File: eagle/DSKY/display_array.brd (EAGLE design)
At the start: 160 x 100 mm, 65 parts, among them IC1 PCF8574T, IC10 PCF8574AT, IC2 PCF8574T, IC3 PCF8574T, IC4 PCF8574T, IC5 PCF8574T, IC6 PCF8574T, IC7 PCF8574T, IC8 PCF8574T, IC9 PCF8574AT

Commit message: brightness control
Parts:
- removed C1, C10, C2, C3, C4, C5, C6, C7, C8, C9: 100n, be_rcl:S_0805
- removed DIS1, DIS2, DIS3, DIS4, DIS5, DIS6, DIS7, DIS8: VQB71, be_opt:T_VQB71
- removed IC1, IC2, IC3, IC4, IC5, IC6, IC7, IC8: PCF8574T, be_i2c:S_SOIC16
- removed IC10, IC9: PCF8574AT, be_i2c:S_SOIC16
- removed LED1, LED12, LED4, LED5, LED7: red, be_opt:S_0805
- removed LED10, LED9: green, be_opt:S_0805
- removed LED2, LED3: blue, be_opt:S_0805
- removed LED6, LED8: yellow, be_opt:S_0805
- removed R1, R2, R3, R4, R5, R6, R7, R8, R9: (no value), be_rcl:S_0805
- removed RN1, RN10, RN11, RN12, RN13, RN14, RN15, RN16, RN2, RN3, RN4, RN5, RN6, RN7, RN8, RN9: 100, be_rcl:T_SIL8
- removed RN17: (no value), be_rcl:T_SIL9
- added C1001, C101, C1205, C1206, C1305, C1306, C201, C301, C401, C501, C601, C701, C801, C901: 100n, be_rcl:S_0805
- added C1201, C1202, C1203, C1204, C1301, C1302, C1303, C1304: 10u, be_rcl:T_RADIAL_5MM_GRID_2.54MM
- added DIS101, DIS201, DIS301, DIS401, DIS501, DIS601, DIS701, DIS801: VQB71, be_opt:T_VQB71
- added H1101, H1102, H1103, H1104: HOLE_4.1_PAD, be_holes:4.1_PAD
- added IC1001, IC901: PCF8574AT, be_i2c:S_SOIC16
- added IC101, IC201, IC301, IC401, IC501, IC601, IC701, IC801: PCF8574T, be_i2c:S_SOIC16
- added IC1201, IC1202, IC1301, IC1302: (no value), be_logic:T_NDIP14
- added LED901, LED902, LED907, LED910, LED911: red, be_opt:S_0805
- added LED903, LED904: green, be_opt:S_0805
- added LED905, LED906: yellow, be_opt:S_0805
- added LED908, LED909: blue, be_opt:S_0805
- added R901, R902, R903, R904, R905, R906, R907, R908, R909: (no value), be_rcl:S_0805
- added RN1001, RN1002, RN101, RN102, RN201, RN202, RN301, RN302, RN401, RN402, RN501, RN502, RN601, RN602, RN701, RN702, RN801, RN802: 100, be_rcl:T_SIL8
- added RN1201, RN1202, RN1301, RN1302: 220, be_rcl:T_SIL8
- added RN1203, RN1303: 4k7, be_rcl:T_SIL8
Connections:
- new net DEBOUNCER_10: C1201.+, RN1201.2, RN1201.3
- new net DEBOUNCER_11: IC1201.1, IC1201.2, RN1201.4, RN1203.3
- new net DEBOUNCER_12: IC1201.3, IC1201.4, IC1201.5
- new net DEBOUNCER_1_OUT#: IC1201.6, RN1001.2, RN1203.4
- new net DEBOUNCER_20: C1202.+, RN1201.6, RN1201.7
- new net DEBOUNCER_21: IC1201.12, IC1201.13, RN1201.8, RN1203.1
- new net DEBOUNCER_22: IC1201.10, IC1201.11, IC1201.9
- new net DEBOUNCER_2_OUT#: IC1201.8, RN1001.4, RN1203.2
- new net DEBOUNCER_30: C1203.+, RN1202.2, RN1202.3
- new net DEBOUNCER_31: IC1202.1, IC1202.2, RN1202.4, RN1203.5
- new net DEBOUNCER_32: IC1202.3, IC1202.4, IC1202.5
- new net DEBOUNCER_3_OUT#: IC1202.6, RN1001.6, RN1203.6
- new net DEBOUNCER_40: C1204.+, RN1202.6, RN1202.7
- new net DEBOUNCER_41: IC1202.12, IC1202.13, RN1202.8, RN1203.7
- new net DEBOUNCER_42: IC1202.10, IC1202.11, IC1202.9
- new net DEBOUNCER_4_OUT#: IC1202.8, RN1001.8, RN1203.8
- new net DEBOUNCER_50: C1301.+, RN1301.2, RN1301.3
- new net DEBOUNCER_51: IC1301.1, IC1301.2, RN1301.4, RN1303.3
- new net DEBOUNCER_52: IC1301.3, IC1301.4, IC1301.5
- new net DEBOUNCER_5_OUT#: IC1301.6, RN1002.2, RN1303.4
- new net DEBOUNCER_60: C1302.+, RN1301.6, RN1301.7
- new net DEBOUNCER_61: IC1301.12, IC1301.13, RN1301.8, RN1303.1
- new net DEBOUNCER_62: IC1301.10, IC1301.11, IC1301.9
- new net DEBOUNCER_6_OUT#: IC1301.8, RN1002.4, RN1303.2
- new net DEBOUNCER_70: C1303.+, RN1302.2, RN1302.3
- new net DEBOUNCER_71: IC1302.1, IC1302.2, RN1302.4, RN1303.5
- new net DEBOUNCER_72: IC1302.3, IC1302.4, IC1302.5
- new net DEBOUNCER_7_OUT#: IC1302.6, RN1002.6, RN1303.6
- new net DEBOUNCER_80: C1304.+, RN1302.6, RN1302.7
- new net DEBOUNCER_81: IC1302.12, IC1302.13, RN1302.8, RN1303.7
- new net DEBOUNCER_82: IC1302.10, IC1302.11, IC1302.9
- new net DEBOUNCER_8_OUT#: IC1302.8, RN1002.8, RN1303.8
- new net IN_1#: RN1201.1
- new net IN_2#: RN1201.5
- new net IN_3#: RN1202.1
- new net IN_4#: RN1202.5
- new net IN_5#: RN1301.1
- new net IN_6#: RN1301.5
- new net IN_7#: RN1302.1
- new net IN_8#: RN1302.5
- net CTRL_SCL: now also IC1001.14, IC101.14, IC201.14, IC301.14, IC401.14, IC501.14, IC601.14, IC701.14, IC801.14, IC901.14; no longer IC1.14, IC10.14, IC2.14, IC3.14, IC4.14, IC5.14, IC6.14, IC7.14, IC8.14, IC9.14
- net CTRL_SDA: now also IC1001.15, IC101.15, IC201.15, IC301.15, IC401.15, IC501.15, IC601.15, IC701.15, IC801.15, IC901.15; no longer IC1.15, IC10.15, IC2.15, IC3.15, IC4.15, IC5.15, IC6.15, IC7.15, IC8.15, IC9.15
- net DRV_1_SEG_A: now also IC101.4, RN101.1; no longer IC1.4, RN1.1
- net DRV_1_SEG_B: now also IC101.5, RN101.3; no longer IC1.5, RN1.3
- net DRV_1_SEG_C: now also IC101.6, RN101.5; no longer IC1.6, RN1.5
- net DRV_1_SEG_D: now also IC101.7, RN101.7; no longer IC1.7, RN1.7
- net DRV_1_SEG_E: now also IC101.9, RN102.1; no longer IC1.9, RN2.1
- net DRV_1_SEG_F: now also IC101.10, RN102.3; no longer IC1.10, RN2.3
- net DRV_1_SEG_G: now also IC101.11, RN102.5; no longer IC1.11, RN2.5
- net DRV_1_SEG_H: now also IC101.12, RN102.7; no longer IC1.12, RN2.7
- net DRV_1_SEG_RA: now also DIS101.7, RN101.2; no longer DIS1.7, RN1.2
- net DRV_1_SEG_RB: now also DIS101.6, RN101.4; no longer DIS1.6, RN1.4
- net DRV_1_SEG_RC: now also DIS101.4, RN101.6; no longer DIS1.4, RN1.6
- net DRV_1_SEG_RD: now also DIS101.2, RN101.8; no longer DIS1.2, RN1.8
- net DRV_1_SEG_RE: now also DIS101.1, RN102.2; no longer DIS1.1, RN2.2
- net DRV_1_SEG_RF: now also DIS101.10, RN102.4; no longer DIS1.10, RN2.4
- net DRV_1_SEG_RG: now also DIS101.9, RN102.6; no longer DIS1.9, RN2.6
- net DRV_1_SEG_RH: now also DIS101.5, RN102.8; no longer DIS1.5, RN2.8
- net DRV_2_SEG_A: now also IC201.4, RN201.1; no longer IC2.4, RN3.1
- net DRV_2_SEG_B: now also IC201.5, RN201.3; no longer IC2.5, RN3.3
- net DRV_2_SEG_C: now also IC201.6, RN201.5; no longer IC2.6, RN3.5
- net DRV_2_SEG_D: now also IC201.7, RN201.7; no longer IC2.7, RN3.7
- net DRV_2_SEG_E: now also IC201.9, RN202.1; no longer IC2.9, RN4.1
- net DRV_2_SEG_F: now also IC201.10, RN202.3; no longer IC2.10, RN4.3
- net DRV_2_SEG_G: now also IC201.11, RN202.5; no longer IC2.11, RN4.5
- net DRV_2_SEG_H: now also IC201.12, RN202.7; no longer IC2.12, RN4.7
- net DRV_2_SEG_RA: now also DIS201.7, RN201.2; no longer DIS2.7, RN3.2
- net DRV_2_SEG_RB: now also DIS201.6, RN201.4; no longer DIS2.6, RN3.4
- net DRV_2_SEG_RC: now also DIS201.4, RN201.6; no longer DIS2.4, RN3.6
- net DRV_2_SEG_RD: now also DIS201.2, RN201.8; no longer DIS2.2, RN3.8
- net DRV_2_SEG_RE: now also DIS201.1, RN202.2; no longer DIS2.1, RN4.2
- net DRV_2_SEG_RF: now also DIS201.10, RN202.4; no longer DIS2.10, RN4.4
- net DRV_2_SEG_RG: now also DIS201.9, RN202.6; no longer DIS2.9, RN4.6
- net DRV_2_SEG_RH: now also DIS201.5, RN202.8; no longer DIS2.5, RN4.8
- net DRV_3_SEG_A: now also IC301.4, RN301.1; no longer IC3.4, RN5.1
- net DRV_3_SEG_B: now also IC301.5, RN301.3; no longer IC3.5, RN5.3
- net DRV_3_SEG_C: now also IC301.6, RN301.5; no longer IC3.6, RN5.5
- net DRV_3_SEG_D: now also IC301.7, RN301.7; no longer IC3.7, RN5.7
- net DRV_3_SEG_E: now also IC301.9, RN302.1; no longer IC3.9, RN6.1
- net DRV_3_SEG_F: now also IC301.10, RN302.3; no longer IC3.10, RN6.3
- net DRV_3_SEG_G: now also IC301.11, RN302.5; no longer IC3.11, RN6.5
- net DRV_3_SEG_H: now also IC301.12, RN302.7; no longer IC3.12, RN6.7
- net DRV_3_SEG_RA: now also DIS301.7, RN301.2; no longer DIS3.7, RN5.2
- net DRV_3_SEG_RB: now also DIS301.6, RN301.4; no longer DIS3.6, RN5.4
- net DRV_3_SEG_RC: now also DIS301.4, RN301.6; no longer DIS3.4, RN5.6
- net DRV_3_SEG_RD: now also DIS301.2, RN301.8; no longer DIS3.2, RN5.8
- net DRV_3_SEG_RE: now also DIS301.1, RN302.2; no longer DIS3.1, RN6.2
- net DRV_3_SEG_RF: now also DIS301.10, RN302.4; no longer DIS3.10, RN6.4
- net DRV_3_SEG_RG: now also DIS301.9, RN302.6; no longer DIS3.9, RN6.6
- net DRV_3_SEG_RH: now also DIS301.5, RN302.8; no longer DIS3.5, RN6.8
- net DRV_4_SEG_A: now also IC401.4, RN401.1; no longer IC4.4, RN7.1
- net DRV_4_SEG_B: now also IC401.5, RN401.3; no longer IC4.5, RN7.3
- net DRV_4_SEG_C: now also IC401.6, RN401.5; no longer IC4.6, RN7.5
- net DRV_4_SEG_D: now also IC401.7, RN401.7; no longer IC4.7, RN7.7
- net DRV_4_SEG_E: now also IC401.9, RN402.1; no longer IC4.9, RN8.1
- net DRV_4_SEG_F: now also IC401.10, RN402.3; no longer IC4.10, RN8.3
- net DRV_4_SEG_G: now also IC401.11, RN402.5; no longer IC4.11, RN8.5
- net DRV_4_SEG_H: now also IC401.12, RN402.7; no longer IC4.12, RN8.7
- net DRV_4_SEG_RA: now also DIS401.7, RN401.2; no longer DIS4.7, RN7.2
- net DRV_4_SEG_RB: now also DIS401.6, RN401.4; no longer DIS4.6, RN7.4
- net DRV_4_SEG_RC: now also DIS401.4, RN401.6; no longer DIS4.4, RN7.6
- net DRV_4_SEG_RD: now also DIS401.2, RN401.8; no longer DIS4.2, RN7.8
- net DRV_4_SEG_RE: now also DIS401.1, RN402.2; no longer DIS4.1, RN8.2
- net DRV_4_SEG_RF: now also DIS401.10, RN402.4; no longer DIS4.10, RN8.4
- net DRV_4_SEG_RG: now also DIS401.9, RN402.6; no longer DIS4.9, RN8.6
- net DRV_4_SEG_RH: now also DIS401.5, RN402.8; no longer DIS4.5, RN8.8
- net DRV_5_SEG_A: now also IC501.4, RN501.1; no longer IC5.4, RN9.1
- net DRV_5_SEG_B: now also IC501.5, RN501.3; no longer IC5.5, RN9.3
- net DRV_5_SEG_C: now also IC501.6, RN501.5; no longer IC5.6, RN9.5
- net DRV_5_SEG_D: now also IC501.7, RN501.7; no longer IC5.7, RN9.7
- net DRV_5_SEG_E: now also IC501.9, RN502.1; no longer IC5.9, RN10.1
- net DRV_5_SEG_F: now also IC501.10, RN502.3; no longer IC5.10, RN10.3
- net DRV_5_SEG_G: now also IC501.11, RN502.5; no longer IC5.11, RN10.5
- net DRV_5_SEG_H: now also IC501.12, RN502.7; no longer IC5.12, RN10.7
- net DRV_5_SEG_RA: now also DIS501.7, RN501.2; no longer DIS5.7, RN9.2
- net DRV_5_SEG_RB: now also DIS501.6, RN501.4; no longer DIS5.6, RN9.4
- net DRV_5_SEG_RC: now also DIS501.4, RN501.6; no longer DIS5.4, RN9.6
- net DRV_5_SEG_RD: now also DIS501.2, RN501.8; no longer DIS5.2, RN9.8
- net DRV_5_SEG_RE: now also DIS501.1, RN502.2; no longer DIS5.1, RN10.2
- net DRV_5_SEG_RF: now also DIS501.10, RN502.4; no longer DIS5.10, RN10.4
- net DRV_5_SEG_RG: now also DIS501.9, RN502.6; no longer DIS5.9, RN10.6
- net DRV_5_SEG_RH: now also DIS501.5, RN502.8; no longer DIS5.5, RN10.8
- net DRV_6_SEG_A: now also IC601.4, RN601.1; no longer IC6.4, RN11.1
- net DRV_6_SEG_B: now also IC601.5, RN601.3; no longer IC6.5, RN11.3
- net DRV_6_SEG_C: now also IC601.6, RN601.5; no longer IC6.6, RN11.5
- net DRV_6_SEG_D: now also IC601.7, RN601.7; no longer IC6.7, RN11.7
- net DRV_6_SEG_E: now also IC601.9, RN602.1; no longer IC6.9, RN12.1
- net DRV_6_SEG_F: now also IC601.10, RN602.3; no longer IC6.10, RN12.3
- net DRV_6_SEG_G: now also IC601.11, RN602.5; no longer IC6.11, RN12.5
- net DRV_6_SEG_H: now also IC601.12, RN602.7; no longer IC6.12, RN12.7
- net DRV_6_SEG_RA: now also DIS601.7, RN601.2; no longer DIS6.7, RN11.2
- net DRV_6_SEG_RB: now also DIS601.6, RN601.4; no longer DIS6.6, RN11.4
- net DRV_6_SEG_RC: now also DIS601.4, RN601.6; no longer DIS6.4, RN11.6
- net DRV_6_SEG_RD: now also DIS601.2, RN601.8; no longer DIS6.2, RN11.8
- net DRV_6_SEG_RE: now also DIS601.1, RN602.2; no longer DIS6.1, RN12.2
- net DRV_6_SEG_RF: now also DIS601.10, RN602.4; no longer DIS6.10, RN12.4
- net DRV_6_SEG_RG: now also DIS601.9, RN602.6; no longer DIS6.9, RN12.6
- net DRV_6_SEG_RH: now also DIS601.5, RN602.8; no longer DIS6.5, RN12.8
- net DRV_7_SEG_A: now also IC701.4, RN701.1; no longer IC7.4, RN13.1
- net DRV_7_SEG_B: now also IC701.5, RN701.3; no longer IC7.5, RN13.3
- net DRV_7_SEG_C: now also IC701.6, RN701.5; no longer IC7.6, RN13.5
- net DRV_7_SEG_D: now also IC701.7, RN701.7; no longer IC7.7, RN13.7
- net DRV_7_SEG_E: now also IC701.9, RN702.1; no longer IC7.9, RN14.1
- net DRV_7_SEG_F: now also IC701.10, RN702.3; no longer IC7.10, RN14.3
- net DRV_7_SEG_G: now also IC701.11, RN702.5; no longer IC7.11, RN14.5
- net DRV_7_SEG_H: now also IC701.12, RN702.7; no longer IC7.12, RN14.7
- net DRV_7_SEG_RA: now also DIS701.7, RN701.2; no longer DIS7.7, RN13.2
- net DRV_7_SEG_RB: now also DIS701.6, RN701.4; no longer DIS7.6, RN13.4
- net DRV_7_SEG_RC: now also DIS701.4, RN701.6; no longer DIS7.4, RN13.6
- net DRV_7_SEG_RD: now also DIS701.2, RN701.8; no longer DIS7.2, RN13.8
- net DRV_7_SEG_RE: now also DIS701.1, RN702.2; no longer DIS7.1, RN14.2
- net DRV_7_SEG_RF: now also DIS701.10, RN702.4; no longer DIS7.10, RN14.4
- net DRV_7_SEG_RG: now also DIS701.9, RN702.6; no longer DIS7.9, RN14.6
- net DRV_7_SEG_RH: now also DIS701.5, RN702.8; no longer DIS7.5, RN14.8
- net DRV_8_SEG_A: now also IC801.4, RN801.1; no longer IC8.4, RN15.1
- net DRV_8_SEG_B: now also IC801.5, RN801.3; no longer IC8.5, RN15.3
- net DRV_8_SEG_C: now also IC801.6, RN801.5; no longer IC8.6, RN15.5
- net DRV_8_SEG_D: now also IC801.7, RN801.7; no longer IC8.7, RN15.7
- net DRV_8_SEG_E: now also IC801.9, RN802.1; no longer IC8.9, RN16.1
- net DRV_8_SEG_F: now also IC801.10, RN802.3; no longer IC8.10, RN16.3
- net DRV_8_SEG_G: now also IC801.11, RN802.5; no longer IC8.11, RN16.5
- net DRV_8_SEG_H: now also IC801.12, RN802.7; no longer IC8.12, RN16.7
- net DRV_8_SEG_RA: now also DIS801.7, RN801.2; no longer DIS8.7, RN15.2
- net DRV_8_SEG_RB: now also DIS801.6, RN801.4; no longer DIS8.6, RN15.4
- net DRV_8_SEG_RC: now also DIS801.4, RN801.6; no longer DIS8.4, RN15.6
- net DRV_8_SEG_RD: now also DIS801.2, RN801.8; no longer DIS8.2, RN15.8
- net DRV_8_SEG_RE: now also DIS801.1, RN802.2; no longer DIS8.1, RN16.2
- net DRV_8_SEG_RF: now also DIS801.10, RN802.4; no longer DIS8.10, RN16.4
- net DRV_8_SEG_RG: now also DIS801.9, RN802.6; no longer DIS8.9, RN16.6
- net DRV_8_SEG_RH: now also DIS801.5, RN802.8; no longer DIS8.5, RN16.8
- net DRV_9_LED_1: now also IC901.4, R901.1, R902.1; no longer IC9.4, R8.1, R9.1
- net DRV_9_LED_2: now also IC901.5, R903.1; no longer IC9.5, R7.1
- net DRV_9_LED_3: now also IC901.6, R904.1; no longer IC9.6, R6.1
- net DRV_9_LED_4: now also IC901.7, R905.1; no longer IC9.7, R5.1
- net DRV_9_LED_5: now also IC901.9, R906.1; no longer IC9.9, R4.1
- net DRV_9_LED_6: now also IC901.10, R907.1; no longer IC9.10, R3.1
- net DRV_9_LED_7: now also IC901.11, R908.1; no longer IC9.11, R2.1
- net DRV_9_LED_8: now also IC901.12, R909.1; no longer IC9.12, R1.1
- net DRV_9_LED_R1A: now also LED901.C, R901.2; no longer LED5.C, R9.2
- net DRV_9_LED_R1B: now also LED902.C, R902.2; no longer LED1.C, R8.2
- net DRV_9_LED_R2: now also LED903.C, R903.2; no longer LED10.C, R7.2
- net DRV_9_LED_R3: now also LED904.C, R904.2; no longer LED9.C, R6.2
- net DRV_9_LED_R4: now also LED905.C, R905.2; no longer LED8.C, R5.2
- net DRV_9_LED_R5: now also LED906.C, R906.2; no longer LED6.C, R4.2
- net DRV_9_LED_R6: now also LED907.C, R907.2; no longer LED7.C, R3.2
- net DRV_9_LED_R7: now also LED908.C, R908.2; no longer LED3.C, R2.2
- net DRV_9_LED_R8: now also LED909.C, R909.2; no longer LED2.C, R1.2
- net DRV_ANODE: now also DIS101.3, DIS101.8, DIS201.3, DIS201.8, DIS301.3, DIS301.8, DIS401.3, DIS401.8, DIS501.3, DIS501.8, DIS601.3, DIS601.8, DIS701.3, DIS701.8, DIS801.3, DIS801.8, LED903.A, LED904.A, LED905.A, LED906.A, LED907.A, LED908.A, LED909.A, LED910.A, LED911.A; no longer DIS1.3, DIS1.8, DIS2.3, DIS2.8, DIS3.3, DIS3.8, DIS4.3, DIS4.8, DIS5.3, DIS5.8, DIS6.3, DIS6.8, DIS7.3, DIS7.8, DIS8.3, DIS8.8
- net GND: now also C1001.1, C101.1, C1201.-, C1202.-, C1203.-, C1204.-, C1205.2, C1206.2, C1301.-, C1302.-, C1303.-, C1304.-, C1305.2, C1306.2, C201.1, C301.1, C401.1, C501.1, C601.1, C701.1, C801.1, C901.1, IC1001.2, IC1001.3, IC1001.8, IC101.1, IC101.2, IC101.3, IC101.8, IC1201.7, IC1202.7, IC1301.7, IC1302.7, IC201.2, IC201.3, IC201.8, IC301.1, IC301.3, IC301.8, IC401.3, IC401.8, IC501.1, IC501.2, IC501.8, IC601.2, IC601.8, IC701.1, IC701.8, IC801.8, IC901.1, IC901.2, IC901.3, IC901.8; no longer C1.1, C10.1, C2.1, C3.1, C4.1, C5.1, C6.1, C7.1, C8.1, C9.1, IC1.1, IC1.2, IC1.3, IC1.8, IC10.2, IC10.3, IC10.8, IC2.2, IC2.3, IC2.8, IC3.1, IC3.3, IC3.8, IC4.3, IC4.8, IC5.1, IC5.2, IC5.8, IC6.2, IC6.8, IC7.1, IC7.8, IC8.8, IC9.1, IC9.2, IC9.3, IC9.8
- net KEYPAD_1_K_1: now also IC1001.4, RN1001.1; no longer IC10.4, RN17.2
- net KEYPAD_1_K_2: now also IC1001.5, RN1001.3; no longer IC10.5, RN17.3
- net KEYPAD_1_K_3: now also IC1001.6, RN1001.5; no longer IC10.6, RN17.4
- net KEYPAD_1_K_4: now also IC1001.7, RN1001.7; no longer IC10.7, RN17.5
- net KEYPAD_1_K_5: now also IC1001.9, RN1002.1; no longer IC10.9, RN17.6
- net KEYPAD_1_K_6: now also IC1001.10, RN1002.3; no longer IC10.10, RN17.7
- net KEYPAD_1_K_7: now also IC1001.11, RN1002.5; no longer IC10.11, RN17.8
- net KEYPAD_1_K_8: now also IC1001.12, RN1002.7; no longer IC10.12, RN17.9
- net N$1: now also LED902.A, LED911.C; no longer LED1.A, LED4.C
- net N$2: now also LED901.A, LED910.C; no longer LED12.C, LED5.A
- net P5V: now also C1001.2, C101.2, C1205.1, C1206.1, C1305.1, C1306.1, C201.2, C301.2, C401.2, C501.2, C601.2, C701.2, C801.2, C901.2, IC1001.1, IC1001.16, IC101.16, IC1201.14, IC1202.14, IC1301.14, IC1302.14, IC201.1, IC201.16, IC301.16, IC301.2, IC401.1, IC401.16, IC401.2, IC501.16, IC501.3, IC601.1, IC601.16, IC601.3, IC701.16, IC701.2, IC701.3, IC801.1, IC801.16, IC801.2, IC801.3, IC901.16; no longer C1.2, C10.2, C2.2, C3.2, C4.2, C5.2, C6.2, C7.2, C8.2, C9.2, IC1.16, IC10.1, IC10.16, IC2.1, IC2.16, IC3.16, IC3.2, IC4.1, IC4.16, IC4.2, IC5.16, IC5.3, IC6.1, IC6.16, IC6.3, IC7.16, IC7.2, IC7.3, IC8.1, IC8.16, IC8.2, IC8.3, IC9.16, LED10.A, LED12.A, LED2.A, LED3.A, LED4.A, LED6.A, LED7.A, LED8.A, LED9.A, RN17.1
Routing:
- net DRV_ANODE: track 140.0 -> 294.7 mm, vias 0 -> 3
- net DRV_9_LED_1: track 20.3 -> 164.2 mm
- net DEBOUNCER_6_OUT#: track 0.00 -> 121.5 mm, vias 0 -> 1
- net DEBOUNCER_7_OUT#: track 0.00 -> 117.0 mm, vias 0 -> 1
- net DEBOUNCER_5_OUT#: track 0.00 -> 109.0 mm
- net DEBOUNCER_8_OUT#: track 0.00 -> 104.5 mm
- net DEBOUNCER_2_OUT#: track 0.00 -> 93.2 mm, vias 0 -> 2
- net DEBOUNCER_1_OUT#: track 0.00 -> 84.1 mm, vias 0 -> 1
- net DEBOUNCER_3_OUT#: track 0.00 -> 73.7 mm, vias 0 -> 1
- net GND: track 125.1 -> 196.4 mm, vias 36 -> 44
- net DEBOUNCER_4_OUT#: track 0.00 -> 48.8 mm, vias 0 -> 1
- net DEBOUNCER_61: track 0.00 -> 46.0 mm
- net DEBOUNCER_21: track 0.00 -> 46.0 mm
- net DRV_9_LED_R2: track 0.00 -> 41.6 mm, vias 0 -> 2
- net DEBOUNCER_80: track 0.00 -> 40.8 mm
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- added copper zone on layer 1, net P5V

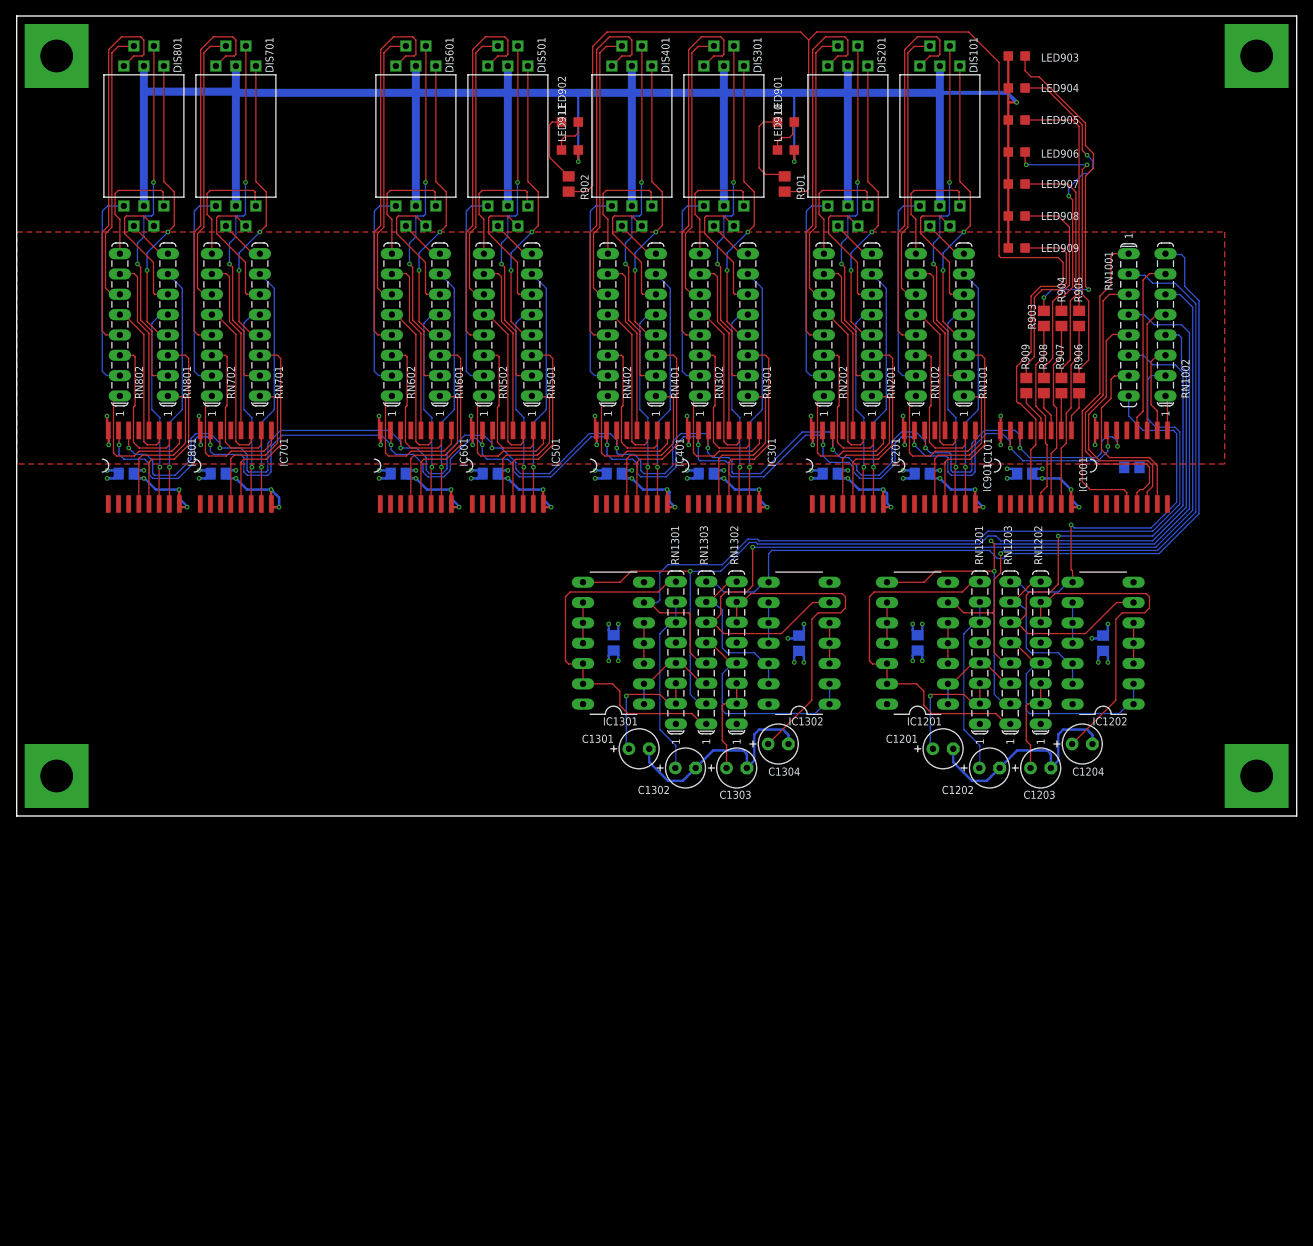
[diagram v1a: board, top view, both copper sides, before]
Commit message: added connectors
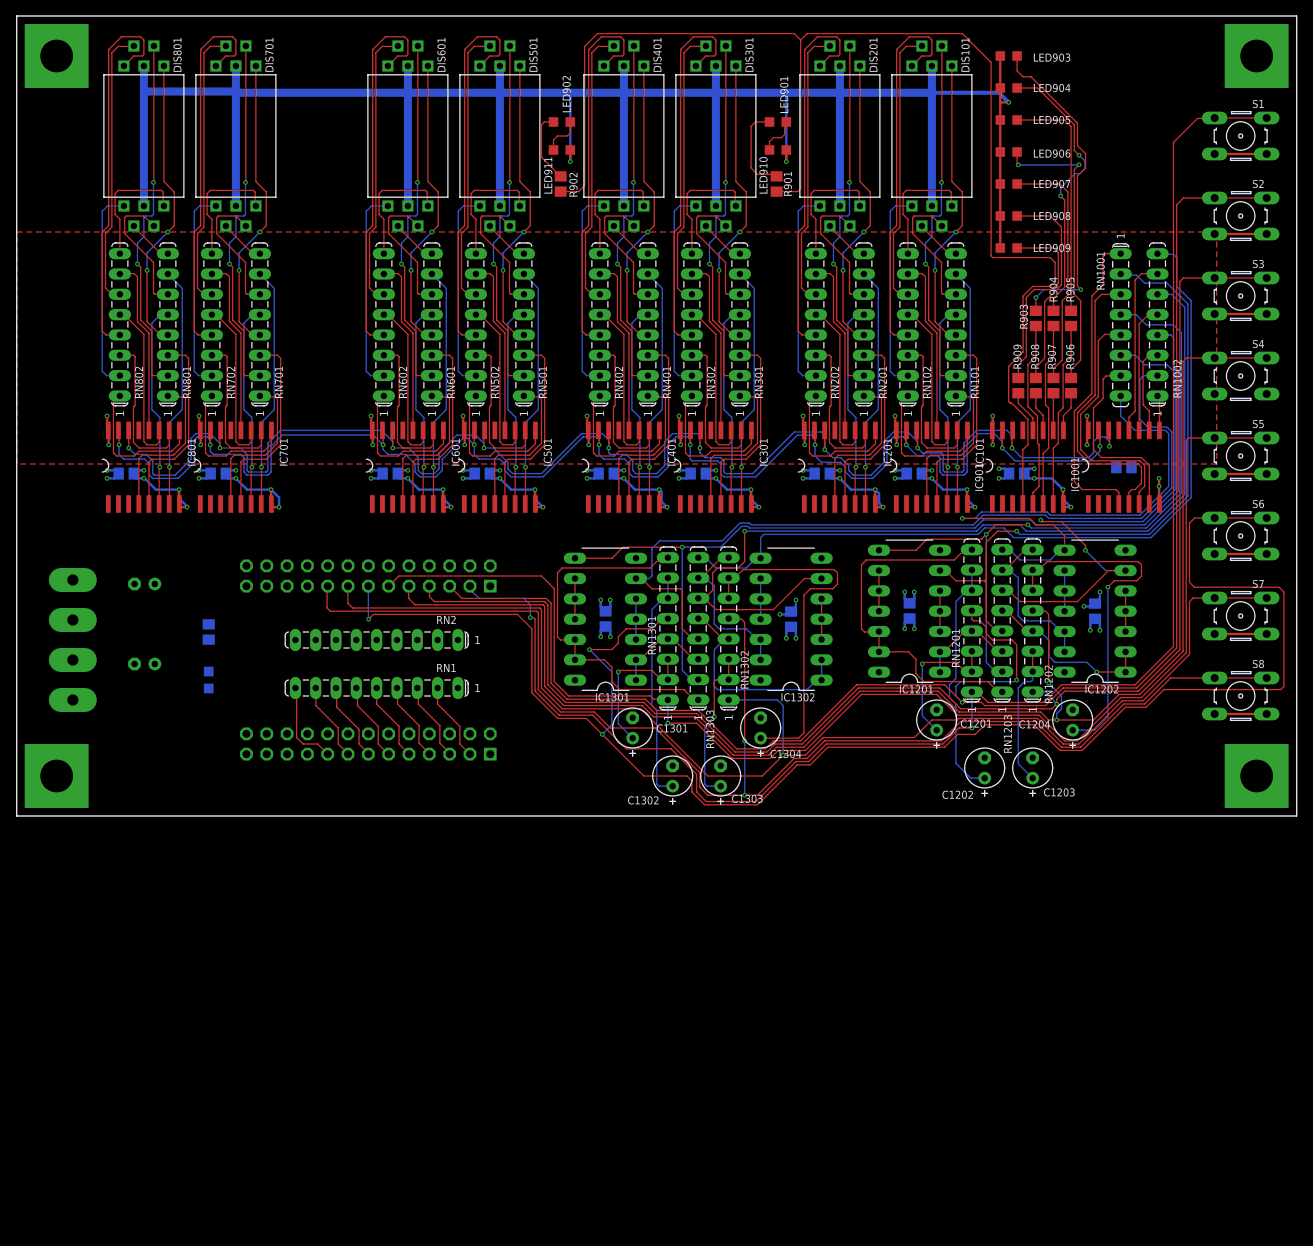
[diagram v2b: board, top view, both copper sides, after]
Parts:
- added C1, C2: 100u, be_rcl:T_RADIAL_7MM_GRID_2.54MM
- added LED1: green, be_opt:S_0805
- added R1: 220, be_rcl:S_0805
- added RN1, RN2: (no value), be_rcl:T_SIL9
- added S1, S2, S3, S4, S5, S6, S7, S8: (no value), be_switch:T_PUSH_BUTTON_6X6
- added X1, X3: MALE_2X13-T-VERTICAL_2.54MM, be_con_jump:T_MALE_2X13_VERTICAL_GRID_2.54MM
- added X2: CLAMP_1X4-T-5MM, be_con_jump:T_WIRE_CLAMP_1X4_5MM
- moved C1205 4.12 mm to (111.6, 25.6)
- moved C1206 4.12 mm to (134.8, 25.6)
- moved IC1201 4.12 mm to (111.6, 25.6)
- moved IC1202 4.12 mm to (134.8, 25.6)
- moved RN1201 4.12 mm to (119.4, 24.4)
- moved RN1202 4.12 mm to (127.0, 24.4)
- moved RN1203 4.12 mm to (123.2, 24.4)
- moved C1201 3.69 mm to (115.0, 12.0), turned to 90 degrees
- moved C1204 3.23 mm to (132.0, 12.0), turned to 90 degrees
- moved C1305 3.16 mm to (73.6, 24.6)
- moved C1306 3.16 mm to (96.8, 24.6)
- moved IC1301 3.16 mm to (73.6, 24.6)
- moved IC1302 3.16 mm to (96.8, 24.6)
- moved RN1301 3.16 mm to (81.4, 23.4)
- moved RN1302 3.16 mm to (89.0, 23.4)
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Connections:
- new net CTRL_ACK#: RN2.3, X1.19
- new net CTRL_B2: RN1.4, X1.7
- new net CTRL_B3: RN1.5, X1.9
- new net CTRL_B4: RN1.6, X1.11
- new net CTRL_B5: RN1.7, X1.13
- new net CTRL_B6: RN1.8, X1.15
- new net CTRL_B7: RN1.9, X1.17
- new net CTRL_BUSY: RN2.4, X1.21
- new net CTRL_STROBE#: RN2.2, X1.1
- new net P5V_LED: LED1.C, R1.2
- net CTRL_SCL: now also RN1.2, X1.3
- net CTRL_SDA: now also RN1.3, X1.5
- net GND: now also C1.-, C2.-, R1.1, S1.1, S1.3, S2.1, S2.3, S3.1, S3.3, S4.1, S4.3, S5.1, S5.3, S6.1, S6.3, S7.1, S7.3, S8.1, S8.3, X1.10, X1.12, X1.14, X1.16, X1.18, X1.2, X1.20, X1.22, X1.24, X1.26, X1.4, X1.6, X1.8, X2.3, X2.4, X3.10, X3.12, X3.14, X3.16, X3.18, X3.2, X3.20, X3.22, X3.24, X3.26, X3.4, X3.6, X3.8
- net IN_1#: now also S1.2, S1.4, X3.3
- net IN_2#: now also S2.2, S2.4, X3.5
- net IN_3#: now also S3.2, S3.4, X3.7
- net IN_4#: now also S4.2, S4.4, X3.9
- net IN_5#: now also S5.2, S5.4, X3.11
- net IN_6#: now also S6.2, S6.4, X3.13
- net IN_7#: now also S7.2, S7.4, X3.15
- net IN_8#: now also S8.2, S8.4, X3.17
- net P5V: now also C1.+, C2.+, LED1.A, RN1.1, RN2.1, X2.1, X2.2
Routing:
- net IN_6#: track 0.00 -> 208.5 mm, vias 0 -> 3
- net IN_2#: track 0.00 -> 202.7 mm, vias 0 -> 2
- net IN_1#: track 0.00 -> 194.5 mm, vias 0 -> 2
- net IN_4#: track 0.00 -> 183.8 mm, vias 0 -> 2
- net IN_3#: track 0.00 -> 177.6 mm, vias 0 -> 1
- net IN_8#: track 0.00 -> 169.1 mm, vias 0 -> 2
- net IN_5#: track 0.00 -> 165.2 mm, vias 0 -> 1
- net IN_7#: track 0.00 -> 160.7 mm, vias 0 -> 1
- net DEBOUNCER_4_OUT#: track 48.8 -> 68.1 mm
- net CTRL_B7: track 0.00 -> 11.0 mm
- net CTRL_B4: track 0.00 -> 9.96 mm
- net CTRL_B6: track 0.00 -> 9.94 mm
- net CTRL_B5: track 0.00 -> 9.94 mm
- net CTRL_B3: track 0.00 -> 9.94 mm
- net CTRL_B2: track 0.00 -> 9.94 mm
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
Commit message: reverse voltage protection
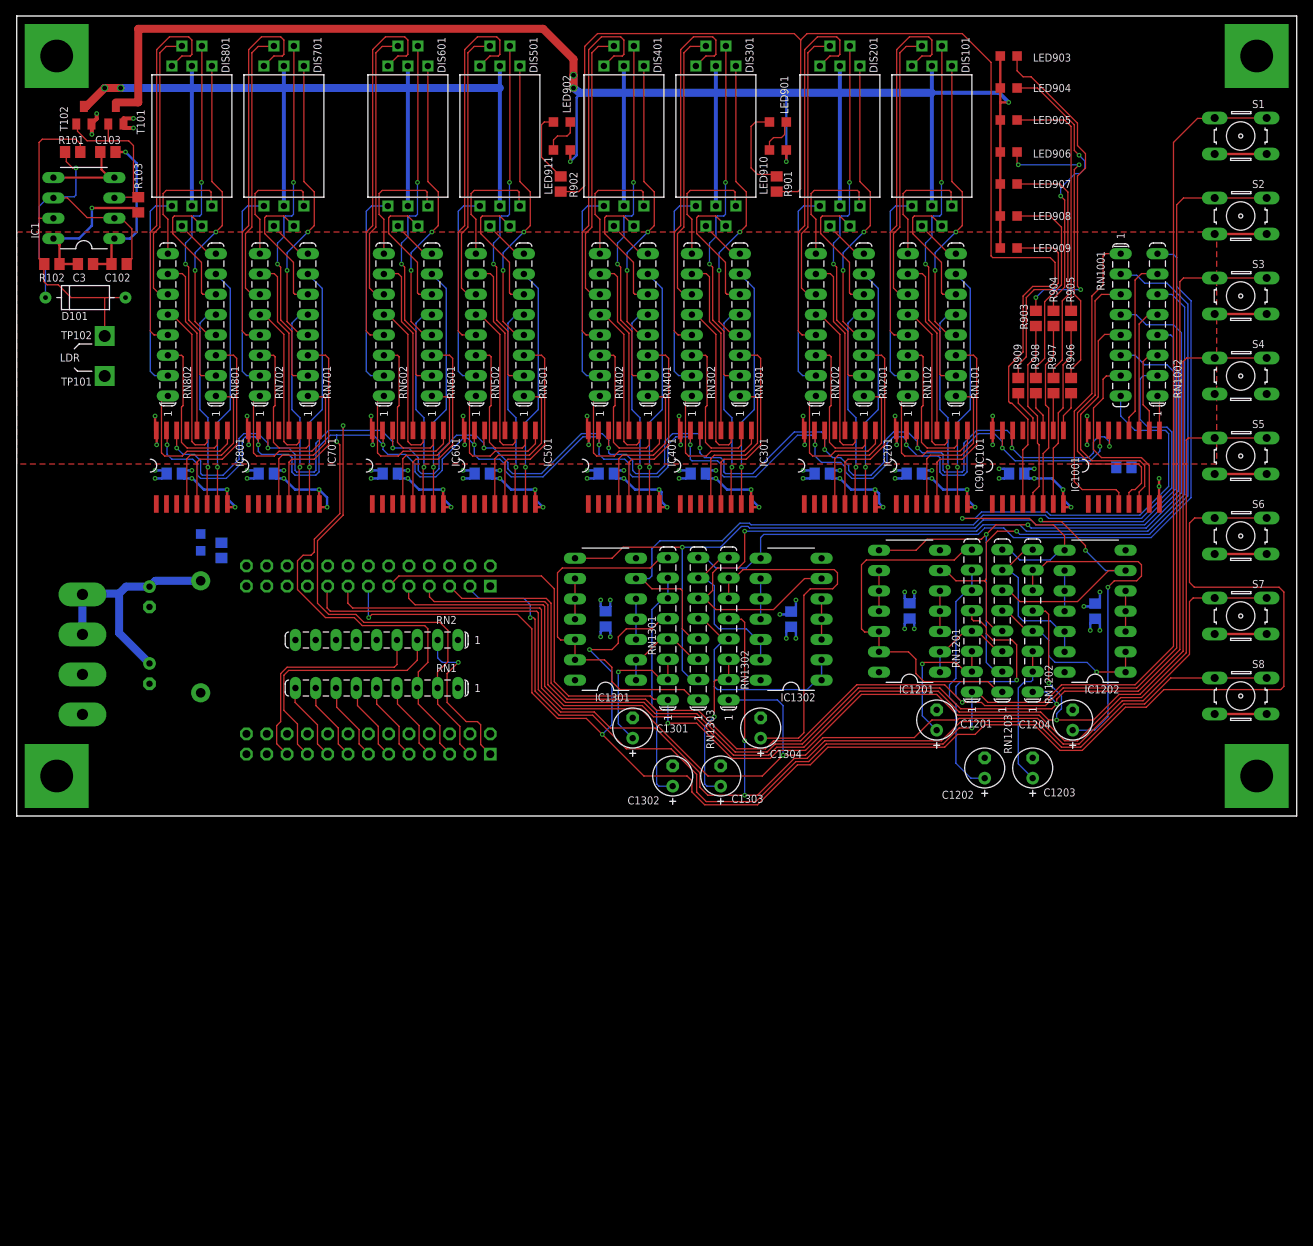
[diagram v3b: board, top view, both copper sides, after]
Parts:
- added C102: 47n, be_rcl:S_0805
- added C103: 10n, be_rcl:S_0805
- added C3: 100n, be_rcl:S_0805
- added D1: (no value), be_diode:T_DO204-2_GRID_14MM
- added D101: BAT48, be_diode:T_DO204_GRID_10MM
- added IC1: NE555V, be_timer:T_NDIP8
- added R101: 10k, be_rcl:S_0805
- added R102: 470k, be_rcl:S_0805
- added R103: 1k, be_rcl:S_0805
- added T101, T102: NX2301P, be_transistor:S_SOT23
- added TP101, TP102: (no value), be_con_jump:T_TEST_POINT_LARGE
- moved LED1 17.2 mm to (23.0, 34.2)
- moved R1 10.3 mm to (25.6, 33.2)
- moved C701 6.00 mm to (31.2, 42.8)
- moved C801 6.00 mm to (19.7, 42.8)
- moved DIS701 6.00 mm to (33.4, 85.0)
- moved IC701 6.00 mm to (33.4, 43.6)
- moved RN701 6.00 mm to (36.4, 61.4)
- moved RN702 6.00 mm to (30.4, 61.4)
- moved RN801 6.00 mm to (24.9, 61.4)
- moved DIS801 6.00 mm to (21.9, 85.0)
- moved IC801 6.00 mm to (21.9, 43.6)
- moved RN802 6.00 mm to (18.9, 61.4)
- moved X2 2.16 mm to (8.20, 20.2)
- moved C1 1.71 mm to (16.6, 27.4), turned to 270 degrees
- moved C2 1.34 mm to (16.6, 17.8), turned to 270 degrees
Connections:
- removed net DRV_ANODE: DIS101.3, DIS101.8, DIS201.3, DIS201.8, DIS301.3, DIS301.8, DIS401.3, DIS401.8, DIS501.3, DIS501.8, DIS601.3, DIS601.8, DIS701.3, DIS701.8, DIS801.3, DIS801.8, LED903.A, LED904.A, LED905.A, LED906.A, LED907.A, LED908.A, LED909.A, LED910.A, LED911.A
- new net DRV_ANODE_1: DIS101.3, DIS101.8, DIS201.3, DIS201.8, DIS301.3, DIS301.8, DIS401.3, DIS401.8, LED903.A, LED904.A, LED905.A, LED906.A, LED907.A, LED908.A, LED909.A, LED910.A, LED911.A, T101.3
- new net DRV_ANODE_2: DIS501.3, DIS501.8, DIS601.3, DIS601.8, DIS701.3, DIS701.8, DIS801.3, DIS801.8, T102.3
- new net TIM_1: C103.1, IC1.4, IC1.5
- new net TIM_2: C102.1, D101.C, IC1.2, IC1.6, R101.1
- new net TIM_3: D101.A, IC1.7, R101.2, R102.1, TP102.1
- new net TIM_OUT: IC1.3, R103.1, T101.1, T102.1
- net GND: now also C102.2, C103.2, C3.2, D1.A, IC1.1
- net P5V: now also C3.1, D1.C, IC1.8, R102.2, R103.2, T101.2, T102.2, TP101.1
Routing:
- net DRV_ANODE: track 293.7 -> 0.00 mm, vias 3 -> 0
- net DRV_ANODE_1: track 0.00 -> 244.4 mm, vias 0 -> 5
- net DRV_ANODE_2: track 0.00 -> 125.0 mm, vias 0 -> 2
- net P5V: track 80.2 -> 137.2 mm, vias 46 -> 51
- net CTRL_SCL: track 214.4 -> 258.0 mm, vias 10 -> 11
- net CTRL_SDA: track 209.6 -> 252.1 mm, vias 10 -> 11
- net TIM_3: track 0.00 -> 42.2 mm
- net TIM_2: track 0.00 -> 39.3 mm, vias 0 -> 1
- net CTRL_ACK#: track 0.00 -> 31.1 mm
- net CTRL_BUSY: track 0.00 -> 28.9 mm
- net GND: track 187.4 -> 208.0 mm, vias 46 -> 47
- net TIM_OUT: track 0.00 -> 20.5 mm
- net CTRL_STROBE#: track 0.00 -> 20.1 mm, vias 0 -> 1
- net TIM_1: track 0.00 -> 11.9 mm
- net CTRL_B7: track 11.0 -> 9.98 mm
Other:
- board text added: "LDR"

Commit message: prepared routing of P5V and GND
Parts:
- removed C1, C2: 100u, be_rcl:T_RADIAL_7MM_GRID_2.54MM
- removed D1: (no value), be_diode:T_DO204-2_GRID_14MM
- removed LED1: green, be_opt:S_0805
- removed R1: 220, be_rcl:S_0805
- added C1401, C1402: 100u, be_rcl:T_RADIAL_7MM_GRID_2.54MM
- added D1401: 1N5400, be_diode:T_DO201_GRID_18MM
- added FD1101, FD1102: FIDUCIAL_CROSSHAIR, be_marks:CROSSHAIR
- added LED1401: green, be_opt:S_0805
- added R1401: 220, be_rcl:S_0805
- IC1201, IC1202, IC1301, IC1302: value (none) -> SN7400N
- R901, R902: value (none) -> 1k5
- R903, R904: value (none) -> 750
- R905, R906: value (none) -> 2k2
- R907: value (none) -> 3k3
- R908, R909: value (none) -> 2k5
- RN1401, RN1402: value (none) -> 10k
- S1501, S1502, S1503, S1504, S1505, S1506, S1507, S1508: value (none) -> set
- TP1601, TP1602: value (none) -> TEST_POINT_T_LARGE
- renumbered C102 to C1602, C103 to C1603, C3 to C1601, D101 to D1601, IC1 to IC1601, R101 to R1601, R102 to R1602, R103 to R1603, RN1 to RN1401, RN2 to RN1402, S1 to S1501, S2 to S1502, S3 to S1503, S4 to S1504, S5 to S1505, S6 to S1506, S7 to S1507, S8 to S1508, T101 to T1601, T102 to T1602, TP101 to TP1601, TP102 to TP1602, X1 to X1402, X2 to X1401, X3 to X1501
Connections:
- net DRV_ANODE_2: now also LED1401.A
- net GND: now also C1401.-, C1402.-, D1401.A, H1101.H1, H1102.H1, H1103.H1, H1104.H1, R1401.1; no longer C1.-, C2.-, D1.A, R1.1
- net P5V: now also C1401.+, C1402.+, D1401.C; no longer C1.+, C2.+, D1.C, LED1.A
- net P5V_LED: now also LED1401.C, R1401.2; no longer LED1.C, R1.2
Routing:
- net DRV_ANODE_2: track 125.0 -> 180.2 mm
- net P5V: track 137.2 -> 111.6 mm
- net P5V_LED: track 0.00 -> 4.04 mm
- net GND: track 208.0 -> 209.6 mm, vias 47 -> 48
